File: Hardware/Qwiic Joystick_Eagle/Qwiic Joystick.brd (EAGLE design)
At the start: 25.4 x 50.8 mm, 41 parts, among them J1 Qwiic Right Angle, J4 Qwiic Right Angle, J6 AVR_SPI_PROG_3X2TESTPOINTS, U1 ATTIN85_SOIC_5.3MM

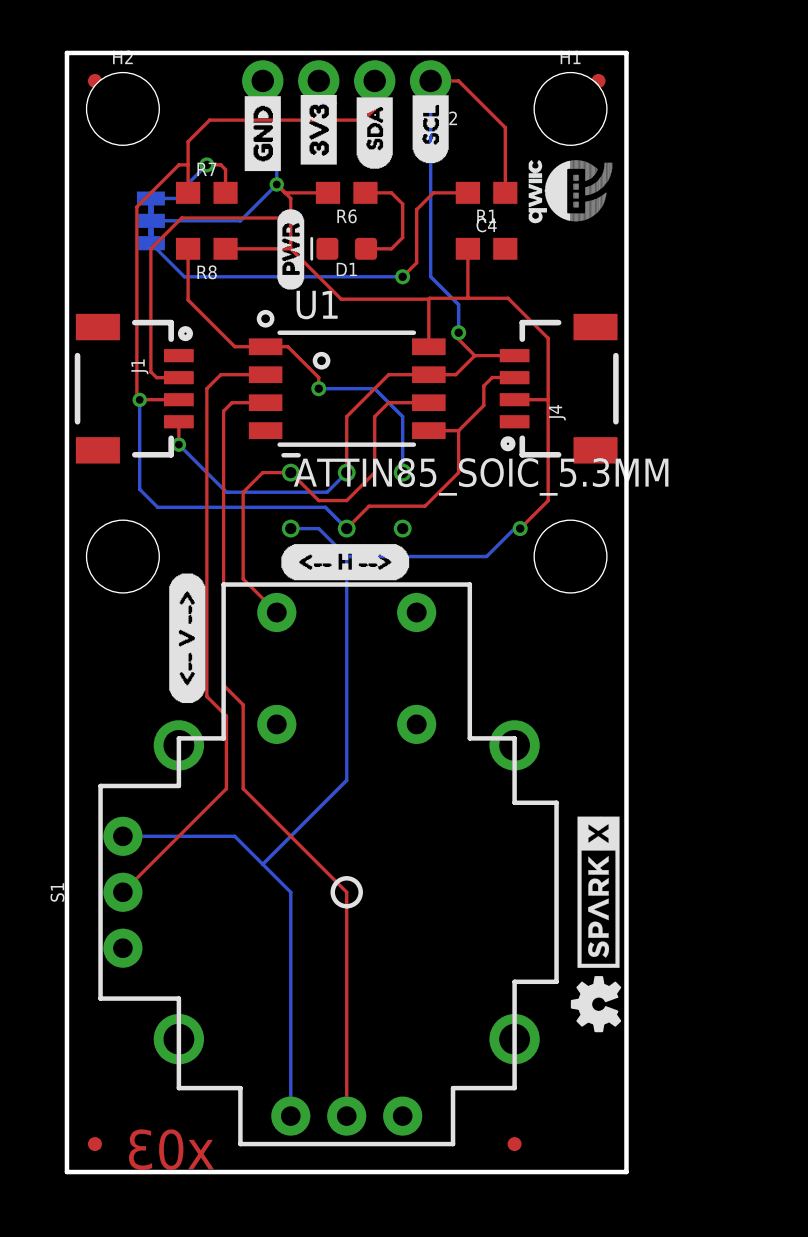
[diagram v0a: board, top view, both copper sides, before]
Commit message: Cleaned repo
Cleaned up the repo, made parts sparkle parts.
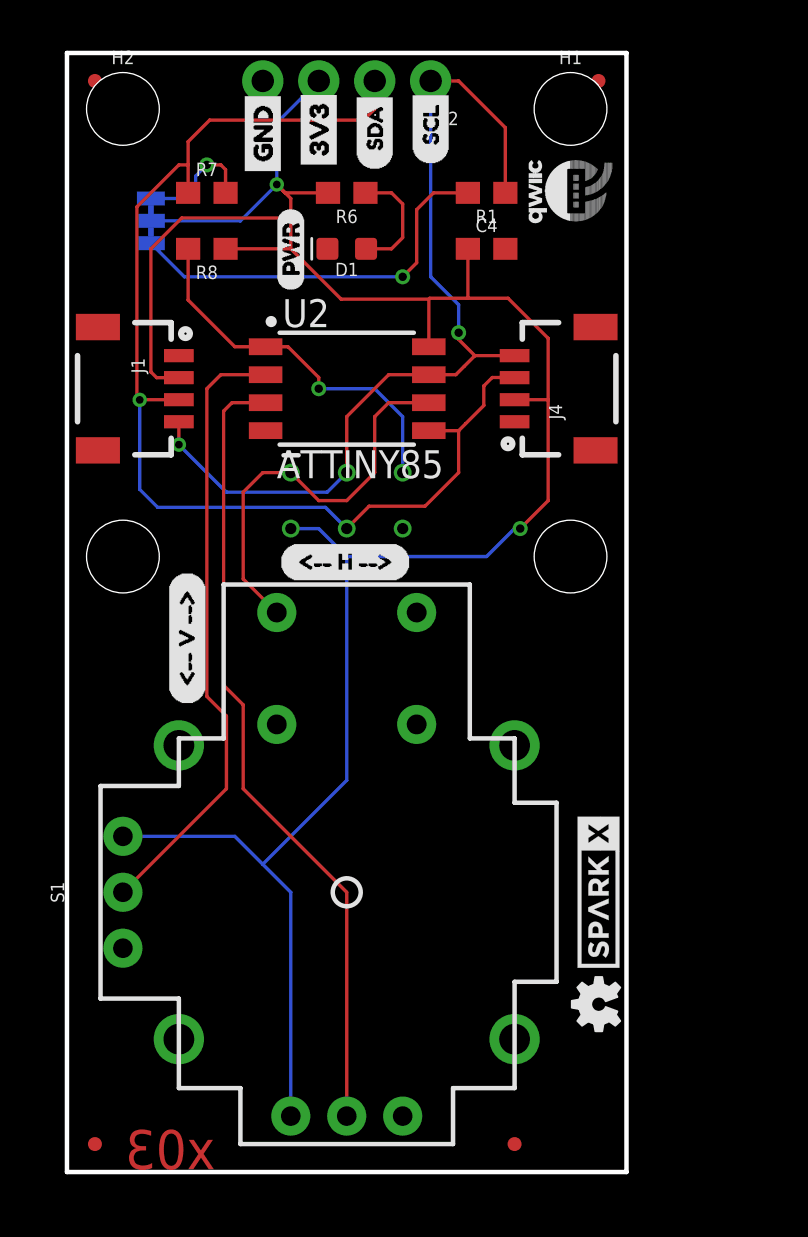
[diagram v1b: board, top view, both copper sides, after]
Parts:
- removed U1: ATTIN85_SOIC_5.3MM, attiny85:ATTINY85
- added U2: ATTINY85, SparkFun-IC-Microcontroller:ATTINY85
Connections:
- net !RST: now also U2.1; no longer U1.1
- net 3.3V: now also U2.8; no longer U1.8
- net GND: now also U2.4; no longer U1.4
- net HORIZONTAL: now also U2.3; no longer U1.3
- net MISO/6/SELECT: now also U2.6; no longer U1.6
- net SCL: now also U2.7; no longer U1.7
- net SDA: now also U2.5; no longer U1.5
- net VERTICAL: now also U2.2; no longer U1.2
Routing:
- net 3.3V: track 106.6 -> 108.8 mm
